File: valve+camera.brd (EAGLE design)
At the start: 65 x 56 mm, 19 parts, among them X1 RASPI_BOARD_B+#_H, X3 5566-4-RIGHTANGLE

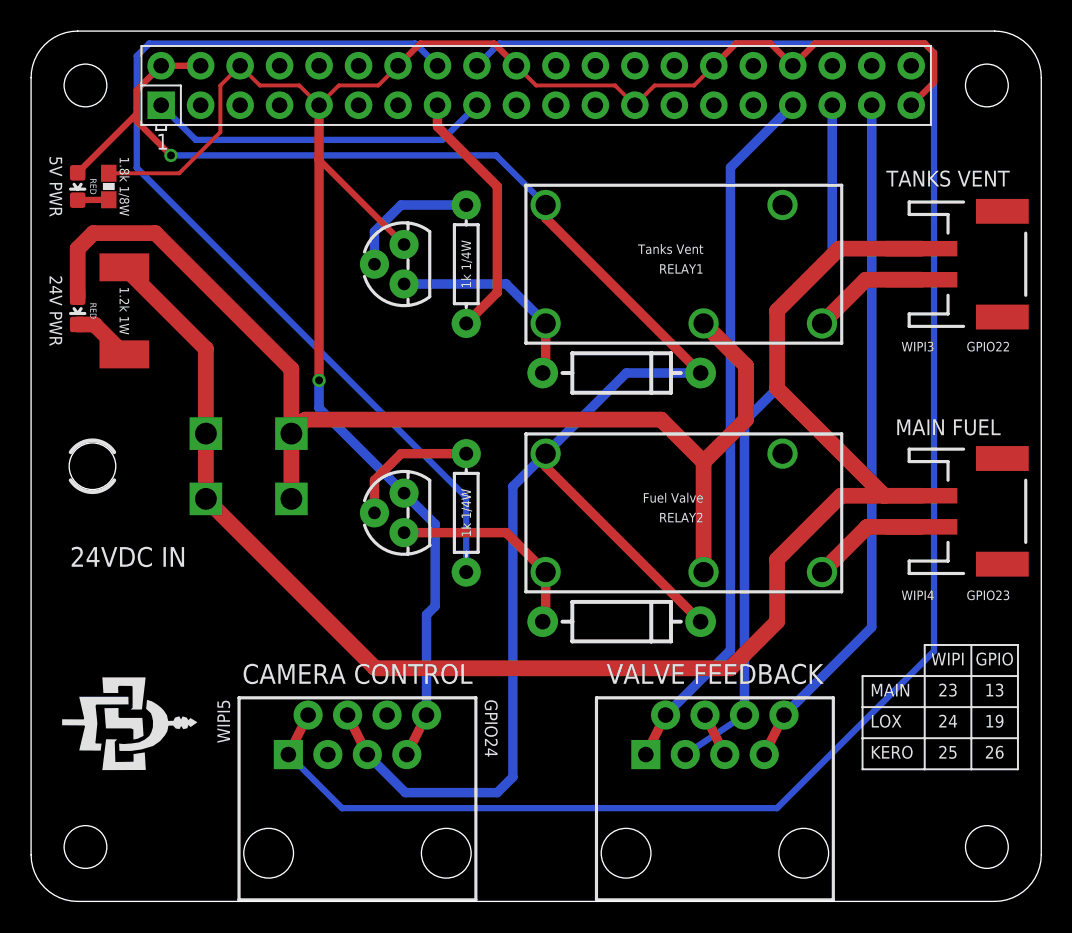
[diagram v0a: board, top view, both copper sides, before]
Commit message: Update camera control wiring and relay components
Updated the components driving the relays to be SMD rather than PTH.
The camera control wiring was updated to have relay activating HackHDs
to be located on this board rather than being located on each Camera
Control board (this means that this board is no longer compatible with
rev1 of the Camera Control board and now requires rev2 or newer).
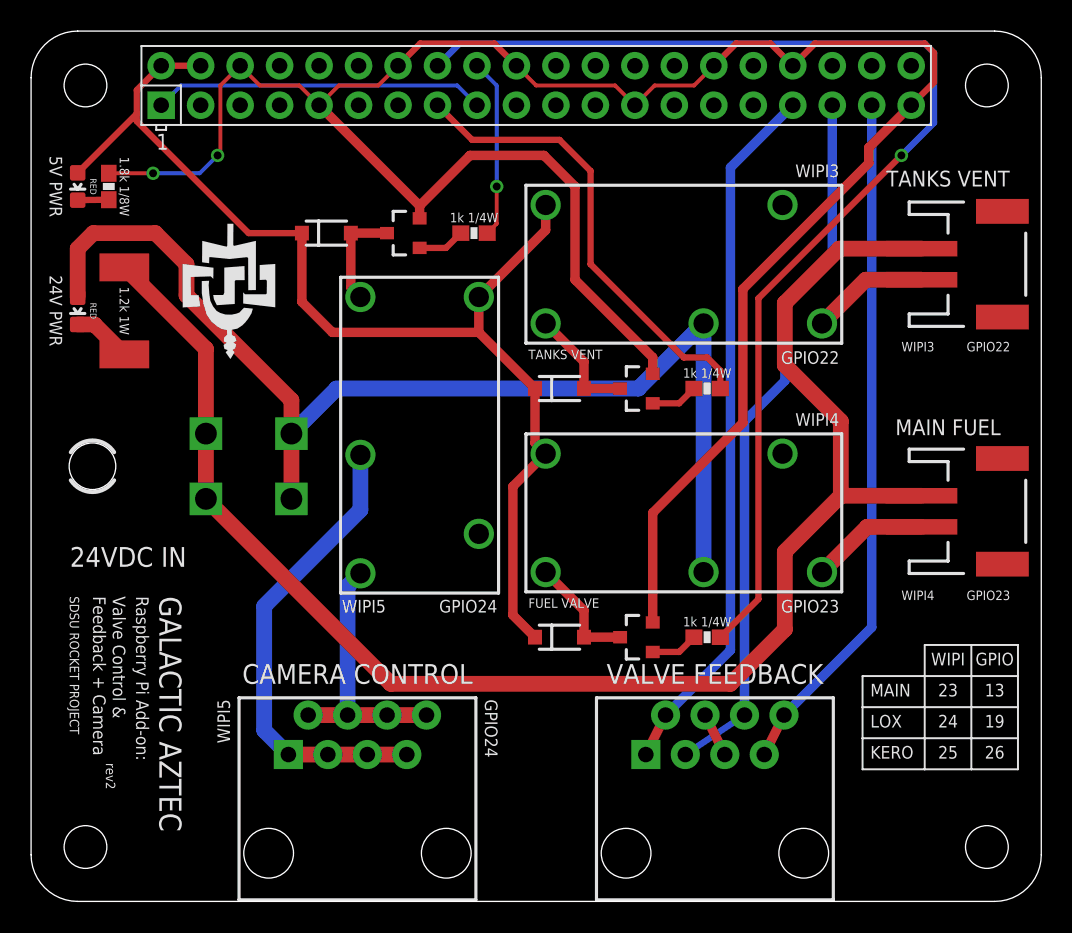
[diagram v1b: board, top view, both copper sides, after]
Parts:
- added D5: RED, SparkFun-LED:LED-0603
- added Q1: (no value), SparkFun-DiscreteSemi:SOT23-3
- added R5: 1.8k 1/8W, SparkFun-Resistors:0603-RES
- added RELAY3: CAMERA CONTROL, SparkFun-Electromechanical:RELAY-G5Q
- D1, D2: device SparkFun-DiscreteSemi:DIODE-1N4001 -> SparkFun-DiscreteSemi:SOD-123
- D3: value RED -> (none); device SparkFun-LED:LED-0603 -> SparkFun-DiscreteSemi:SOD-123
- Q2, Q4: device SparkFun-DiscreteSemi:TO-92 -> SparkFun-DiscreteSemi:SOT23-3
- R1, R2: device SparkFun-Resistors:AXIAL-0.3 -> SparkFun-Passives:0603-RES
- R3: value 1.2k 1W -> 1k 1/4W; device SparkFun-Resistors:R2512 -> SparkFun-Passives:0603-RES
- R4: value 1.8k 1/8W -> 1.2k 1W; device SparkFun-Resistors:0603-RES -> SparkFun-Resistors:R2512
- RELAY1: value Tanks Vent -> TANKS VENT
- RELAY2: value Fuel Valve -> FUEL VALVE
- moved R3 23.0 mm to (28.5, 43.0), turned to 180 degrees
- moved R1 17.4 mm to (43.5, 33.0), turned to 180 degrees
- moved R2 17.4 mm to (43.5, 17.0), turned to 180 degrees
- moved Q2 17.0 mm to (39.0, 33.0)
- moved Q4 17.0 mm to (39.0, 17.0)
- moved D3 16.8 mm to (19.0, 43.0), turned to 0 degrees
- moved R4 8.06 mm to (6.00, 38.0)
- moved D4 8.00 mm to (3.00, 38.0)
- moved D1 4.12 mm to (34.0, 33.0)
- moved D2 4.12 mm to (34.0, 17.0)
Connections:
- removed net N$1 (its old number): D3.C, R3.1
- new net CIN: RELAY3.2, RJ45-1.1, RJ45-1.3, RJ45-1.5, RJ45-1.7
- new net COUT: RELAY3.3, RJ45-1.2, RJ45-1.4, RJ45-1.6, RJ45-1.8
- new net N$2: D5.C, R5.1
- new net N$5: Q1.1, R3.2
- new net N$6: D3.A, Q1.3, RELAY3.1
- net 24V: now also D4.A; no longer D3.A
- net 5V: now also D3.C, D5.A, RELAY3.5; no longer D4.A, RJ45-1.4, RJ45-1.5
- net GND: now also Q1.2, Q2.2, Q4.2, R5.2; no longer Q2.3, Q4.3, R4.2, RJ45-1.7, RJ45-1.8
- net GND2: now also R4.2; no longer R3.2
- net N$3: now also Q2.1, R1.2; no longer Q2.2, R1.P$2
- net N$4: now also Q2.3; no longer Q2.1
- net N$7: now also Q4.1, R2.2; no longer Q4.2, R2.P$2
- net N$8: now also Q4.3; no longer Q4.1
- net WIPI3: now also R1.1; no longer R1.P$1
- net WIPI4: now also R2.1; no longer R2.P$1
- net WIPI5: now also R3.1; no longer RJ45-1.1, RJ45-1.2
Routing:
- net WIPI5: track 118.7 -> 11.5 mm, vias 0 -> 1
- net 5V: track 118.0 -> 75.2 mm, vias 1 -> 0
- net CIN: track 0.00 -> 30.1 mm
- net GND: track 122.3 -> 146.3 mm, vias 1 -> 2
- net COUT: track 0.00 -> 17.1 mm
- net WIPI4: track 62.3 -> 76.1 mm, vias 0 -> 1
- net WIPI3: track 16.5 -> 29.9 mm
- net N$6: track 0.00 -> 6.69 mm
- net N$4: track 13.4 -> 7.54 mm
- net N$8: track 13.4 -> 7.54 mm
- net N$3: track 8.71 -> 3.04 mm
- net N$7: track 8.71 -> 3.04 mm
- net N$1 (its old number): track 3.80 -> 0.00 mm
- net N$5: track 0.00 -> 3.04 mm
- net N$2: track 0.00 -> 2.00 mm
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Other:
- board text added: "Feedback + Camera"
- board text added: "Valve Control &"
- board text added: "rev2"
- board text removed: "Valve + Camera Control"
- board text removed: "Valve Control/Feedback + Camera Control"
- board text removed: "rev1"

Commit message: Fix feedback port and power thru hole size
Feedback ethernet port was fixed by adding a missing trace.
The 24VDC in thru hole size diameter was increased to adhere to the
datasheet's specifications.
The JST plugs used for valve actuation (tanks vent and main fuel) were
change from SMD to PTH as we had problems with the SMD connectors
breaking off when connecting or disconnecting the plugs.
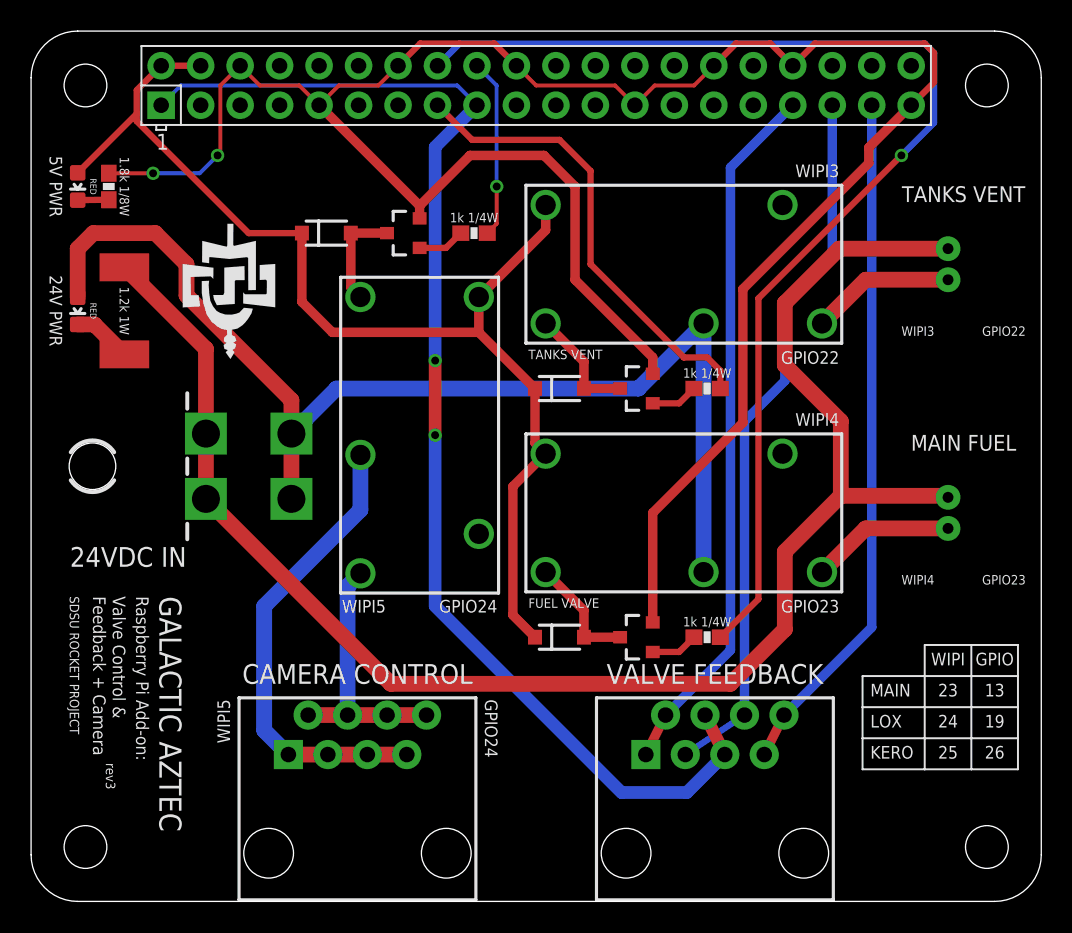
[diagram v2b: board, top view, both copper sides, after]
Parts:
- removed JP2, JP3: M02-JST-2MM-SMT, SparkFun-Connectors:JST-2-SMD
- removed X3: 5566-4-RIGHTANGLE, SDSURocket-BreakoutBoards:5566-4
- added JP1, JP4: (no value), SparkFun-Connectors:JST-2-PTH-NS
- added X2: 5566-4-RIGHTANGLE, SDSURocket-Connectors:5566-4
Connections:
- removed net 3V3: RJ45-2.4, RJ45-2.5
- net 24V: now also X2.3, X2.4; no longer X3.3, X3.4
- net 3.3V: now also RJ45-2.4, RJ45-2.5
- net GND2: now also JP1.1, JP4.1, X2.1, X2.2; no longer JP2.1, JP3.1, X3.1, X3.2
- net NO1: now also JP1.2; no longer JP2.2
- net NO2: now also JP4.2; no longer JP3.2
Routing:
- net 3.3V: track 21.4 -> 82.2 mm, vias 0 -> 2
- net GND2: track 100.1 -> 103.6 mm
- net 3V3: track 2.84 -> 0.00 mm
- net NO1: track 7.57 -> 9.27 mm
- net NO2: track 7.62 -> 9.27 mm
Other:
- board text added: "rev3"
- board text removed: "rev2"
